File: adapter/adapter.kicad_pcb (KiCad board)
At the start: 2 copper layers, 43.5 x 38.6 mm, 26 parts, among them J1 Conn_01x06_Female, J2 Conn_01x01_Female, J5 Conn_01x01_Female, SW1 RotaryEncoder_Switch

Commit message: tailor
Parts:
- removed ? (x3): , 
- removed J2, J5: Conn_01x01_Female, Library:1_PinHeader
- removed JP1: SolderJumper_3_Open, Library:SolderJumper-3_P1.3mm_Open_RoundedPad1.0x1.5mm
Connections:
- Dcol1 pad 2: Net-(Dcol1-Pad2) -> Net-(Dcol1-A)
- J1 pad 1: Vcc -> Gnd
- J1 pad 2: button -> r1
- J1 pad 4: r1 -> unconnected-(J1-Pin_4-Pad4)
- J1 pad 5: DIN -> button
- J1 pad 6: Gnd -> Col
- SW1 pad S1: Net-(JP1-Pad2) -> Net-(Dcol1-A)
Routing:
- net Gnd: track 43.1 -> 11.6 mm, vias 1 -> 0
- net DOUT: track 14.4 -> 0.00 mm
- net Net-(Dcol1-Pad2): track 12.0 -> 0.00 mm
- net Net-(Dcol1-A): track 0.00 -> 7.71 mm
- net Col: track 9.40 -> 14.7 mm
- net button: track 23.9 -> 19.2 mm
- net Vcc: track 4.26 -> 0.00 mm
- net DIN: track 4.51 -> 0.84 mm
- net Net-(JP1-Pad2): track 3.17 -> 0.00 mm
- net r2: track 33.3 -> 30.4 mm
- net r1: track 34.2 -> 32.2 mm, vias 0 -> 1
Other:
- board text added: "REV Oli 0"
- board text added: "ROW"
- board text added: "x"
- board text removed: "BTN"
- board text removed: "DIN"
- board text removed: "DO"
- board text removed: "REV 1.2"
- board text removed: "VCC"

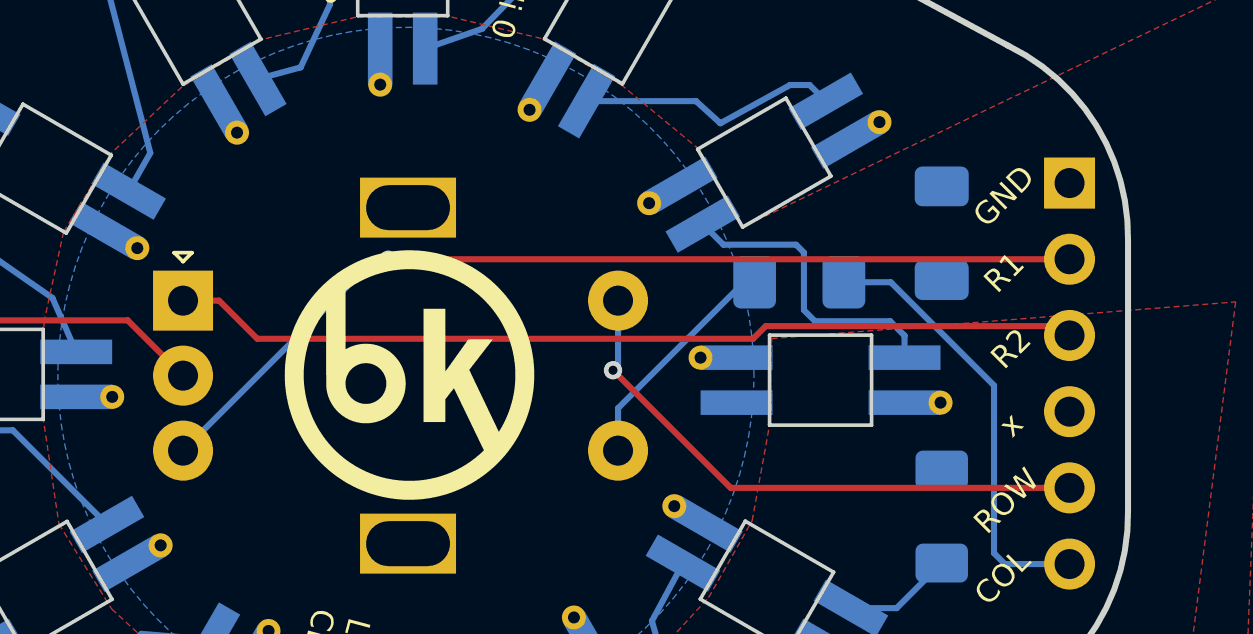
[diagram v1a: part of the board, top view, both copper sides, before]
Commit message: rearrange to avoid cable twist
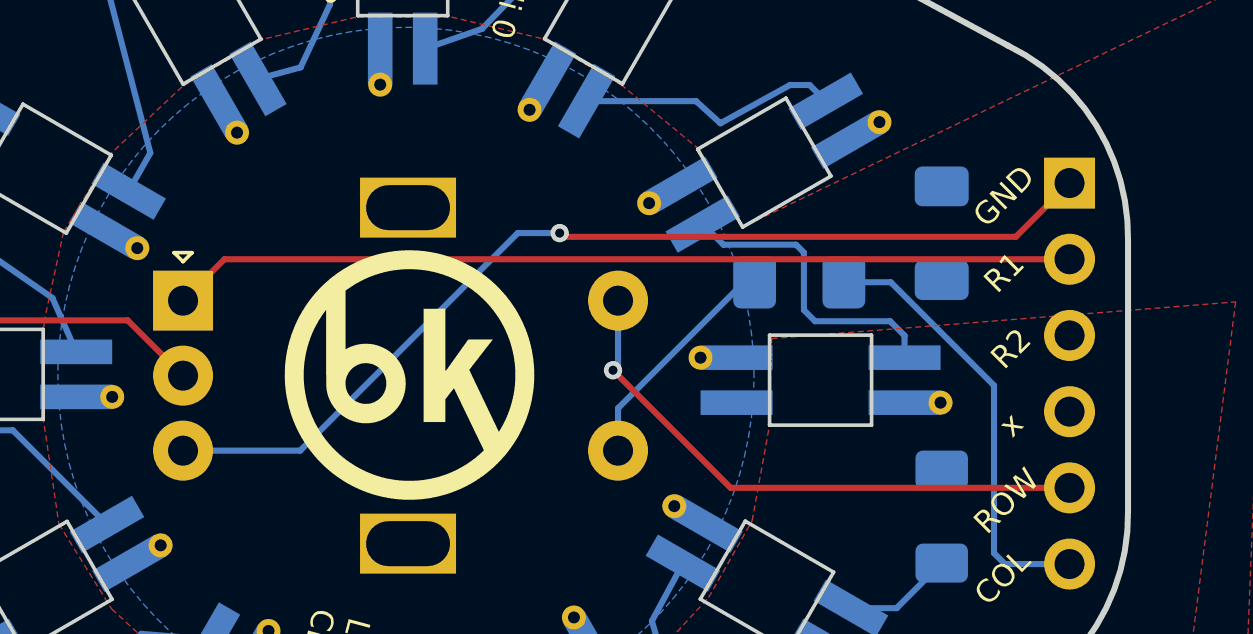
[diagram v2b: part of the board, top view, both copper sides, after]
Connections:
- J1 pad 1: Gnd -> r1
- J1 pad 2: r1 -> r2
- J1 pad 3: r2 -> Gnd
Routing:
- net r1: track 32.2 -> 33.3 mm
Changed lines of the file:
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@@
       (stroke (width 0.1) (type solid)) (layer "F.Fab"))
     (pad "1" thru_hole rect locked (at 0 -6.42) (size 1.7 1.7) (drill 1) (layers "*.Cu" "*.Mask")
-      (net 2 "Gnd") (pinfunction "Pin_1") (pintype "passive"))
+      (net 17 "r1") (pinfunction "Pin_1") (pintype "passive"))
     (pad "2" thru_hole oval locked (at 0 -3.88) (size 1.7 1.7) (drill 1) (layers "*.Cu" "*.Mask")
-      (net 17 "r1") (pinfunction "Pin_2") (pintype "passive"))
+      (net 18 "r2") (pinfunction "Pin_2") (pintype "passive"))
     (pad "3" thru_hole oval locked (at 0 -1.34) (size 1.7 1.7) (drill 1) (layers "*.Cu" "*.Mask")
-      (net 18 "r2") (pinfunction "Pin_3") (pintype "passive"))
+      (net 2 "Gnd") (pinfunction "Pin_3") (pintype "passive"))
     (pad "4" thru_hole oval locked (at 0 1.2) (size 1.7 1.7) (drill 1) (layers "*.Cu" "*.Mask")
       (net 22 "unconnected-(J1-Pin_4-Pad4)") (pinfunction "Pin_4") (pintype "passive"))
@@
   (gr_circle (center 52.5 43.6) (end 67 56.85)
     (stroke (width 0.1) (type solid)) (fill none) (layer "F.Fab"))
-  (gr_text "R2" (at 72.583426 42.687764 45) (layer "B.SilkS")
+  (gr_text "GND" (at 72.583426 42.687764 45) (layer "B.SilkS")
     (effects (font (size 0.75 0.75) (thickness 0.1)) (justify mirror))
   )
@@
     (effects (font (size 0.75 0.75) (thickness 0.1)) (justify mirror))
   )
-  (gr_text "R1" (at 72.356141 40.147765 45) (layer "B.SilkS")
+  (gr_text "R2" (at 72.356141 40.147765 45) (layer "B.SilkS")
     (effects (font (size 0.75 0.75) (thickness 0.1)) (justify mirror))
   )
@@
     (effects (font (size 0.75 0.75) (thickness 0.1)) (justify mirror))
   )
-  (gr_text "GND" (at 72.343514 37.607765 45) (layer "B.SilkS")
+  (gr_text "R1" (at 72.343514 37.607765 45) (layer "B.SilkS")
     (effects (font (size 0.75 0.75) (thickness 0.1)) (justify mirror))
   )
@@
   (segment (start 59.5 43.252) (end 59.332 43.42) (width 0.2032) (layer "B.Cu") (net 16))
   (segment (start 59.5 41.1) (end 59.5 43.252) (width 0.2032) (layer "B.Cu") (net 16))
-  (segment (start 51.839 39.737) (end 51.856 39.72) (width 0.2032) (layer "F.Cu") (net 17))
-  (segment (start 51.856 39.72) (end 74.55 39.72) (width 0.2032) (layer "F.Cu") (net 17))
-  (via (at 51.839 39.737) (size 0.6096) (drill 0.3048) (layers "F.Cu" "B.Cu") (net 17))
-  (segment (start 45 46.1) (end 51.363 39.737) (width 0.2032) (layer "B.Cu") (net 17))
-  (segment (start 51.363 39.737) (end 51.839 39.737) (width 0.2032) (layer "B.Cu") (net 17))
-  (segment (start 45 41.1) (end 46.2032 41.1) (width 0.2032) (layer "F.Cu") (net 18))
-  (segment (start 64.425073 41.9484) (end 74.2384 41.9484) (width 0.2032) (layer "F.Cu") (net 18))
-  (segment (start 64.002073 42.3714) (end 64.425073 41.9484) (width 0.2032) (layer "F.Cu") (net 18))
-  (segment (start 47.4746 42.3714) (end 64.002073 42.3714) (width 0.2032) (layer "F.Cu") (net 18))
-  (segment (start 74.2384 41.9484) (end 74.55 42.26) (width 0.2032) (layer "F.Cu") (net 18))
-  (segment (start 46.2032 41.1) (end 47.4746 42.3714) (width 0.2032) (layer "F.Cu") (net 18))
+  (segment (start 57.554 38.848) (end 57.678695 38.972695) (width 0.2032) (layer "F.Cu") (net 17))
+  (segment (start 57.678695 38.972695) (end 72.757305 38.972695) (width 0.2032) (layer "F.Cu") (net 17))
+  (segment (start 72.757305 38.972695) (end 74.55 37.18) (width 0.2032) (layer "F.Cu") (net 17))
+  (via (at 57.554 38.848) (size 0.6096) (drill 0.3048) (layers "F.Cu" "B.Cu") (net 17))
+  (segment (start 56.157 38.848) (end 48.905 46.1) (width 0.2032) (layer "B.Cu") (net 17))
+  (segment (start 57.554 38.848) (end 56.157 38.848) (width 0.2032) (layer "B.Cu") (net 17))
+  (segment (start 48.905 46.1) (end 45 46.1) (width 0.2032) (layer "B.Cu") (net 17))
+  (segment (start 46.38 39.72) (end 74.55 39.72) (width 0.2032) (layer "F.Cu") (net 18))
+  (segment (start 45 41.1) (end 46.38 39.72) (width 0.2032) (layer "F.Cu") (net 18))
   (segment (start 70.882 47.34) (end 70.289 46.747) (width 0.2032) (layer "B.Cu") (net 19))
   (segment (start 72.032 43.928) (end 72.032 49.516) (width 0.2032) (layer "B.Cu") (net 20))
